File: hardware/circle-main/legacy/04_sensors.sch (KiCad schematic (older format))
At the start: 3 parts, among them J20 KEYED_PPG_HEAD, U20 ICM-42688-P

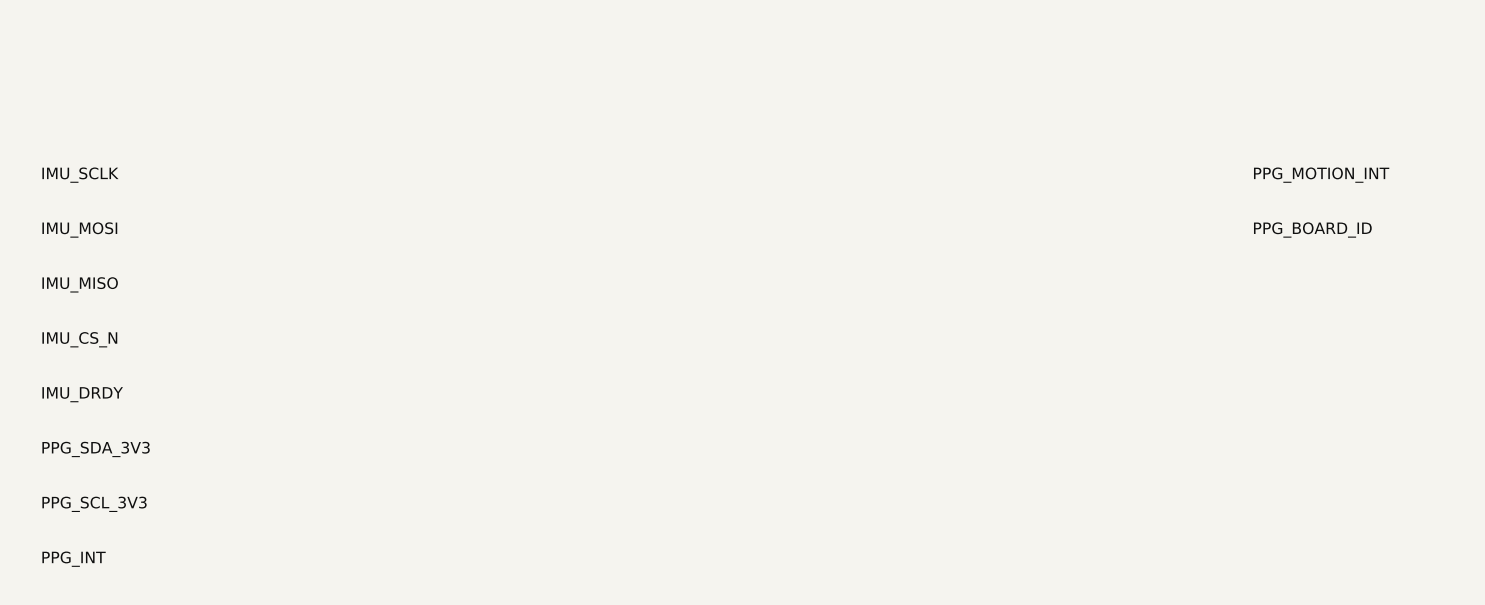
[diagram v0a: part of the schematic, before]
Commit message: Make every CIRCLE review claim reproducible
Validate and export the architecture-level schematics with KiCad 10.0.5, add zero-violation ERC gates, engineering documentation, and one-command evidence hashing.

Constraint: KiCad CLI does not import legacy .sch into native .kicad_sch

Rejected: Hand-written native S-expressions | would create unvalidated CAD

Confidence: medium

Scope-risk: broad

Reversibility: clean

Directive: Treat NET annotations as architecture interfaces, not fabrication-ready connectivity

Tested: py -3.11 tools/verify_release.py; 30 tests; KiCad 10.0.5 ERC/BOM/PDF/SVG/netlist exports

Not-tested: Native conversion, PCB layout, footprints, powered electrodes, human connection, EMC, or regulatory compliance
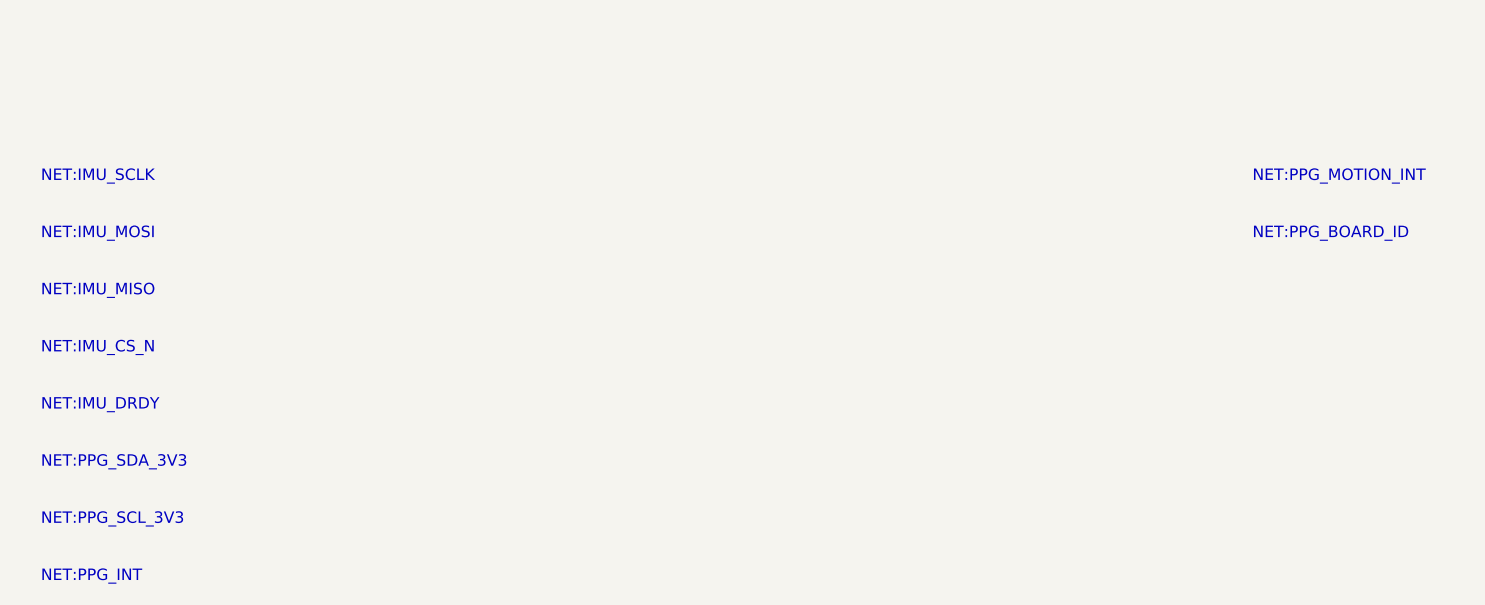
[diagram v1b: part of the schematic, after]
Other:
- note added: "NET:IMU_CS_N"
- note added: "NET:IMU_DRDY"
- note added: "NET:IMU_MISO"
- note added: "NET:IMU_MOSI"
- note added: "NET:IMU_SCLK"
- note added: "NET:PPG_BOARD_ID"
- note added: "NET:PPG_INT"
- note added: "NET:PPG_MOTION_INT"
- note added: "NET:PPG_SCL_3V3"
- note added: "NET:PPG_SDA_3V3"
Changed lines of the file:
@@
 Sheet 1 1
 Title "IMU and optical-head interface"
+Date "2026-08-14"
+Rev "A"
+Comp "Vers3Dynamics"
 Comment1 "ENGINEERING REVIEW ONLY - NOT FOR HUMAN CONNECTION"
+Comment2 "Generated artifact - edit manifest/generator"
+Comment3 ""
+Comment4 ""
 $EndDescr
 $Comp
@@
 F 0 "U20" H 1400 1300 50  0000 C CNN
 F 1 "ICM-42688-P" H 1400 1100 50  0000 C CNN
+F 2 "" H 1300 1200 50  0001 C CNN
+F 3 "" H 1300 1200 50  0001 C CNN
+	1    1300 1200
 	1    0    0    -1
 $EndComp
@@
 F 0 "J20" H 3500 1300 50  0000 C CNN
 F 1 "KEYED_PPG_HEAD" H 3500 1100 50  0000 C CNN
+F 2 "" H 3400 1200 50  0001 C CNN
+F 3 "" H 3400 1200 50  0001 C CNN
+	1    3400 1200
 	1    0    0    -1
 $EndComp
@@
 F 0 "D20" H 5600 1300 50  0000 C CNN
 F 1 "PPG_CABLE_ESD_BAT_DOMAIN" H 5600 1100 50  0000 C CNN
+F 2 "" H 5500 1200 50  0001 C CNN
+F 3 "" H 5500 1200 50  0001 C CNN
+	1    5500 1200
 	1    0    0    -1
 $EndComp
-Text Label 700 5600 0    50   ~ 0
-IMU_SCLK
-Text Label 700 5840 0    50   ~ 0
-IMU_MOSI
-Text Label 700 6080 0    50   ~ 0
-IMU_MISO
-Text Label 700 6320 0    50   ~ 0
-IMU_CS_N
-Text Label 700 6560 0    50   ~ 0
-IMU_DRDY
-Text Label 700 6800 0    50   ~ 0
-PPG_SDA_3V3
-Text Label 700 7040 0    50   ~ 0
-PPG_SCL_3V3
-Text Label 700 7280 0    50   ~ 0
-PPG_INT
-Text Label 6000 5600 0    50   ~ 0
-PPG_MOTION_INT
-Text Label 6000 5840 0    50   ~ 0
-PPG_BOARD_ID
 Text Notes 600 400 0    50   ~ 0
 ENGINEERING REVIEW ONLY - NOT FOR HUMAN CONNECTION
+Text Notes 700 5600 0    50   ~ 0
+NET:IMU_SCLK
+Text Notes 700 5850 0    50   ~ 0
+NET:IMU_MOSI
+Text Notes 700 6100 0    50   ~ 0
+NET:IMU_MISO
+Text Notes 700 6350 0    50   ~ 0
+NET:IMU_CS_N
+Text Notes 700 6600 0    50   ~ 0
+NET:IMU_DRDY
+Text Notes 700 6850 0    50   ~ 0
+NET:PPG_SDA_3V3
+Text Notes 700 7100 0    50   ~ 0
+NET:PPG_SCL_3V3
+Text Notes 700 7350 0    50   ~ 0
+NET:PPG_INT
+Text Notes 6000 5600 0    50   ~ 0
+NET:PPG_MOTION_INT
+Text Notes 6000 5850 0    50   ~ 0
+NET:PPG_BOARD_ID
 $EndSCHEMATC
